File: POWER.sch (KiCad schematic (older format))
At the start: 34 parts, among them U201 TPS61021A, U402 MAX1555

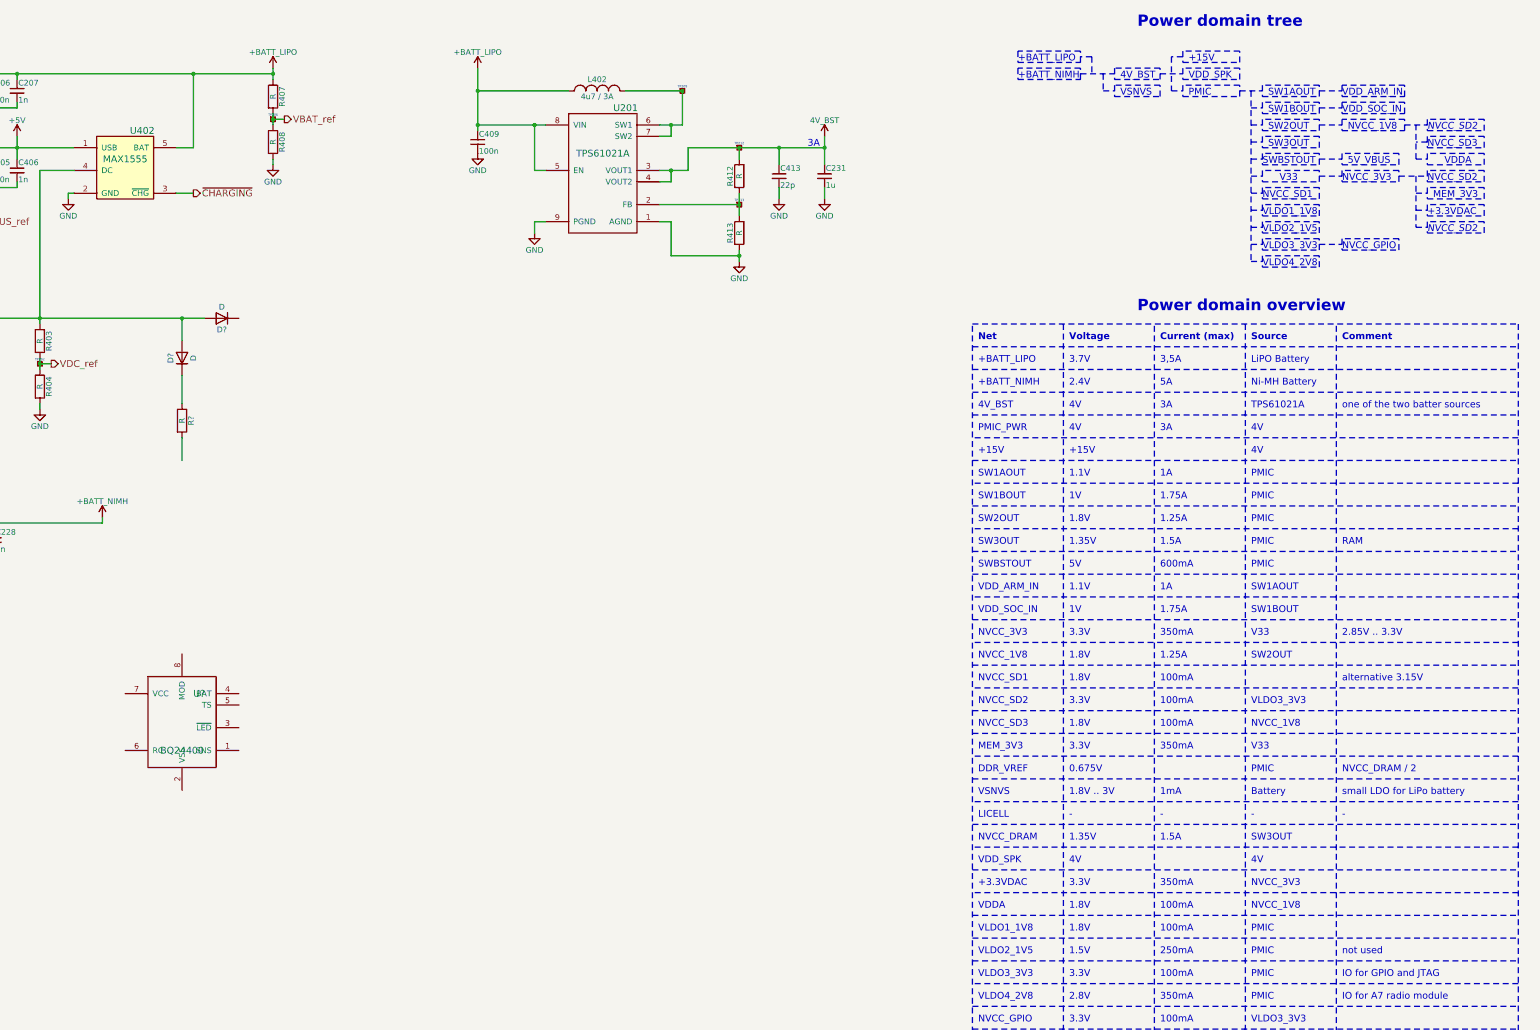
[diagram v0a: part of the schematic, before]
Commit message: on battery charging circuit for NiMH battery
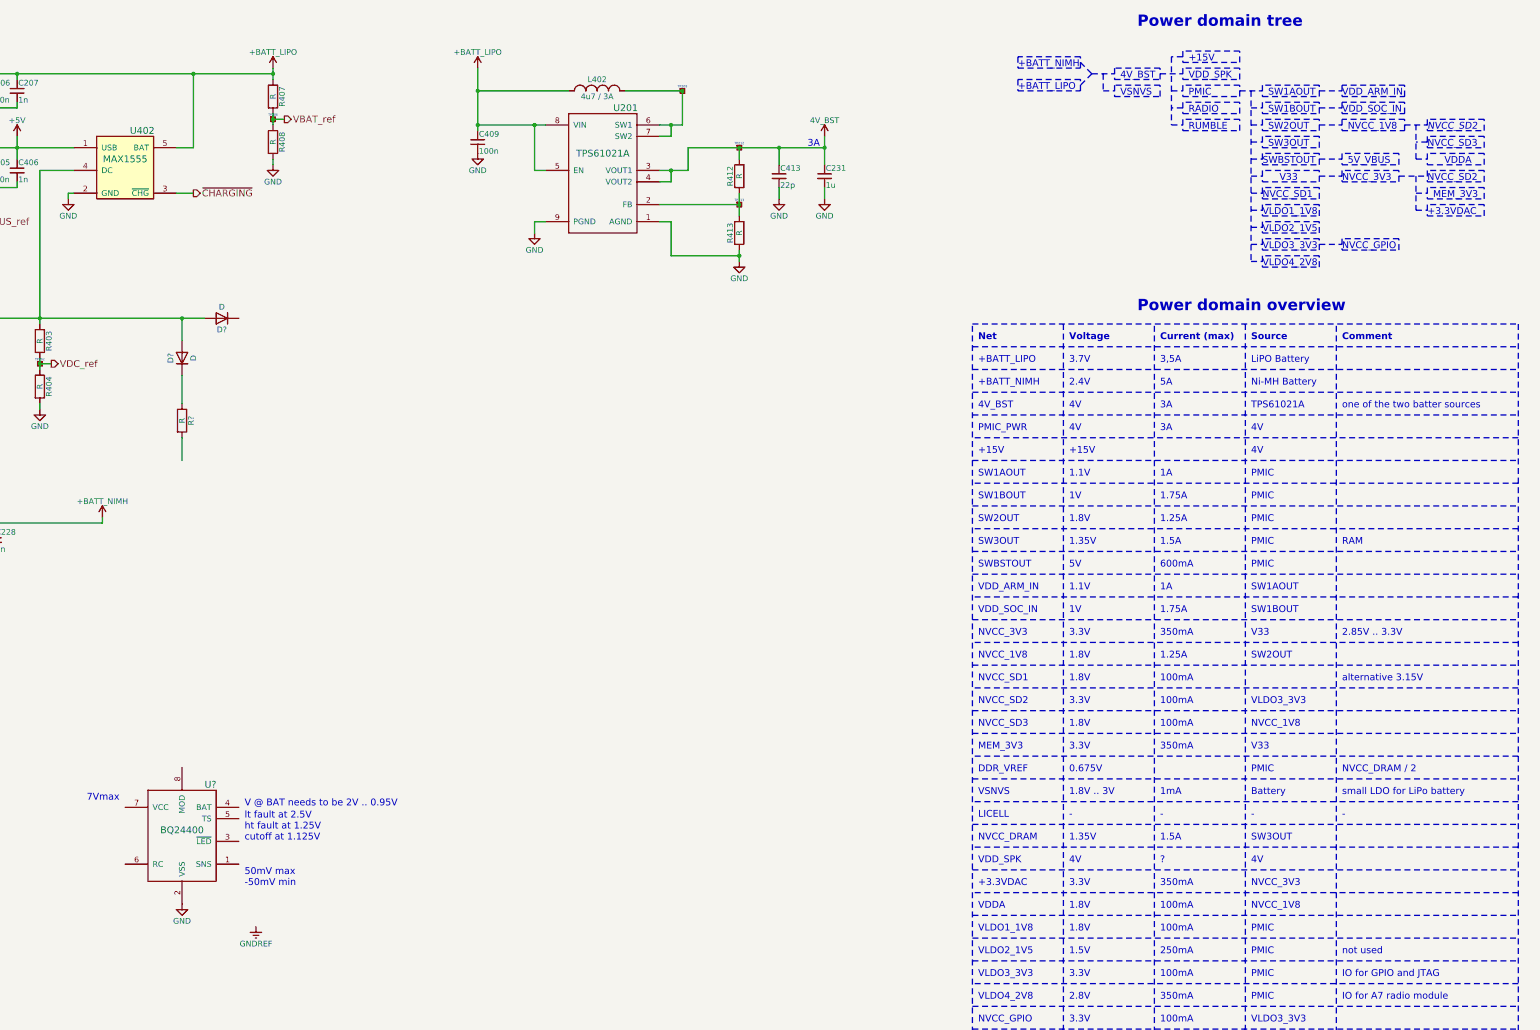
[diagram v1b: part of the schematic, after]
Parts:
- removed U?: BQ24400, symbol BQ24400
- added U?: BQ24400, symbol BQ24400
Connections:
- net GND: now also U?.2 (VSS)
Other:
- note added: "50mV max\n-50mV min"
- note added: "7Vmax"
- note added: "?"
- note added: "RADIO"
- note added: "RUMBLE"
- note added: "V @ BAT needs to be 2V .. 0.95V"
- note added: "lt fault at 2.5V\nht fault at 1.25V\ncutoff at 1.125V\n"
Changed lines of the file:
@@
-$EndComp
-$Comp
-L BQ24400 U?
-U 1 1 59571401
-P 4200 6900
-F 0 "U?" H 4350 7150 60  0000 C CNN
-F 1 "BQ24400" H 4200 6650 60  0000 C CNN
-F 2 "" H 4200 6900 60  0001 C CNN
-F 3 "" H 4200 6900 60  0001 C CNN
-	1    4200 6900
-	1    0    0    -1
 $EndComp
 $Comp
@@
 Text Notes 13600 8150 0    60   ~ 0
 4V
-Text Notes 11550 1100 0    60   ~ 0
+Text Notes 11550 1350 0    60   ~ 0
 +BATT_LIPO
-Text Notes 11550 1250 0    60   ~ 0
+Text Notes 11550 1150 0    60   ~ 0
 +BATT_NIMH
 Text Notes 12450 1250 0    60   ~ 0
@@
 Text Notes 14400 9350 0    60   ~ 0
 IO for A7 radio module
-Text Notes 15150 2600 0    60   Italic 0
-NVCC_SD2
 Text Notes 12600 800  0    99   ~ 20
 Power domain tree
@@
 	3500 5150 3500 5100
 Wire Notes Line
-	12100 1200 12400 1200
+	12200 1200 12400 1200
 Wire Notes Line
 	12400 1150 12400 1250
@@
 	13000 1050 12900 1050
 Wire Notes Line
-	12900 1050 12900 1350
+	12900 1050 12900 1650
 Wire Notes Line
 	12900 1350 13000 1350
@@
 	15050 1950 15050 1650
 Wire Notes Line
-	15050 2100 15050 2550
-Wire Notes Line
-	15050 2550 15150 2550
-Wire Notes Line
-	15150 2500 15150 2600
-Wire Notes Line
-	15150 2600 15650 2600
-Wire Notes Line
-	15650 2600 15650 2500
-Wire Notes Line
-	15650 2500 15150 2500
-Wire Notes Line
-	11550 1100 12100 1100
-Wire Notes Line
-	12100 1100 12100 1000
-Wire Notes Line
-	12100 1000 11550 1000
-Wire Notes Line
-	11550 1000 11550 1100
-Wire Notes Line
-	11550 1150 11550 1250
-Wire Notes Line
-	11550 1250 12100 1250
-Wire Notes Line
-	12100 1250 12100 1150
-Wire Notes Line
-	12100 1150 11550 1150
-Wire Notes Line
-	12200 1050 12100 1050
-Wire Notes Line
-	12200 1050 12200 1200
+	11550 1350 12100 1350
+Wire Notes Line
+	12100 1350 12100 1250
+Wire Notes Line
+	12100 1250 11550 1250
+Wire Notes Line
+	11550 1250 11550 1350
+Wire Notes Line
+	11550 1050 11550 1150
+Wire Notes Line
+	11550 1150 12100 1150
+Wire Notes Line
+	12100 1150 12100 1050
+Wire Notes Line
+	12100 1050 11550 1050
+Wire Notes Line
+	12200 1200 12100 1300
+Wire Notes Line
+	12100 1100 12200 1200
 Wire Notes Line
 	11150 3400 15950 3400
@@
 Text Notes 13600 6950 0    60   ~ 0
 NVCC_1V8
+Text Notes 13050 1550 0    60   ~ 0
+RADIO
+Wire Notes Line
+	13000 1500 12900 1500
+Wire Notes Line
+	13000 1450 13000 1550
+Wire Notes Line
+	13000 1550 13500 1550
+Wire Notes Line
+	13500 1550 13500 1450
+Wire Notes Line
+	13500 1450 13000 1450
+Text Notes 13050 1700 0    60   ~ 0
+RUMBLE
+Wire Notes Line
+	12900 1650 13000 1650
+Wire Notes Line
+	13000 1600 13000 1700
+Wire Notes Line
+	13000 1700 13500 1700
+Wire Notes Line
+	13500 1700 13500 1600
+Wire Notes Line
+	13500 1600 13000 1600
+Wire Notes Line
+	15050 2100 15050 2400
+Text Notes 12800 8150 0    60   ~ 0
+?
+$Comp
+L BQ24400 U?
+U 1 1 595CC806
+P 4200 7900
+F 0 "U?" H 4450 8350 60  0000 C CNN
+F 1 "BQ24400" H 4200 7950 60  0000 C CNN
+F 2 "" H 4850 7850 60  0001 C CNN
+F 3 "" H 4850 7850 60  0001 C CNN
+	1    4200 7900
+	1    0    0    -1
+$EndComp
+Text Notes 4750 7650 0    60   ~ 0
+V @ BAT needs to be 2V .. 0.95V
+Text Notes 4750 8350 0    60   ~ 0
+50mV max\n-50mV min
+Text Notes 3650 7600 2    60   ~ 0
+7Vmax
+Text Notes 4750 7950 0    60   ~ 0
+lt fault at 2.5V\nht fault at 1.25V\ncutoff at 1.125V\n
+$Comp
+L GND #PWR?
+U 1 1 595CEE09
+P 4200 8500
+F 0 "#PWR?" H 4200 8250 50  0001 C CNN
+F 1 "GND" H 4200 8350 50  0000 C CNN
+F 2 "" H 4200 8500 50  0000 C CNN
+F 3 "" H 4200 8500 50  0000 C CNN
+	1    4200 8500
+	1    0    0    -1
+$EndComp
+$Comp
+L GNDREF #PWR?
+U 1 1 595CF102
+P 4850 8700
+F 0 "#PWR?" H 4850 8450 50  0001 C CNN
+F 1 "GNDREF" H 4850 8550 50  0000 C CNN
+F 2 "" H 4850 8700 50  0000 C CNN
+F 3 "" H 4850 8700 50  0000 C CNN
+	1    4850 8700
+	1    0    0    -1
+$EndComp
 $EndSCHEMATC

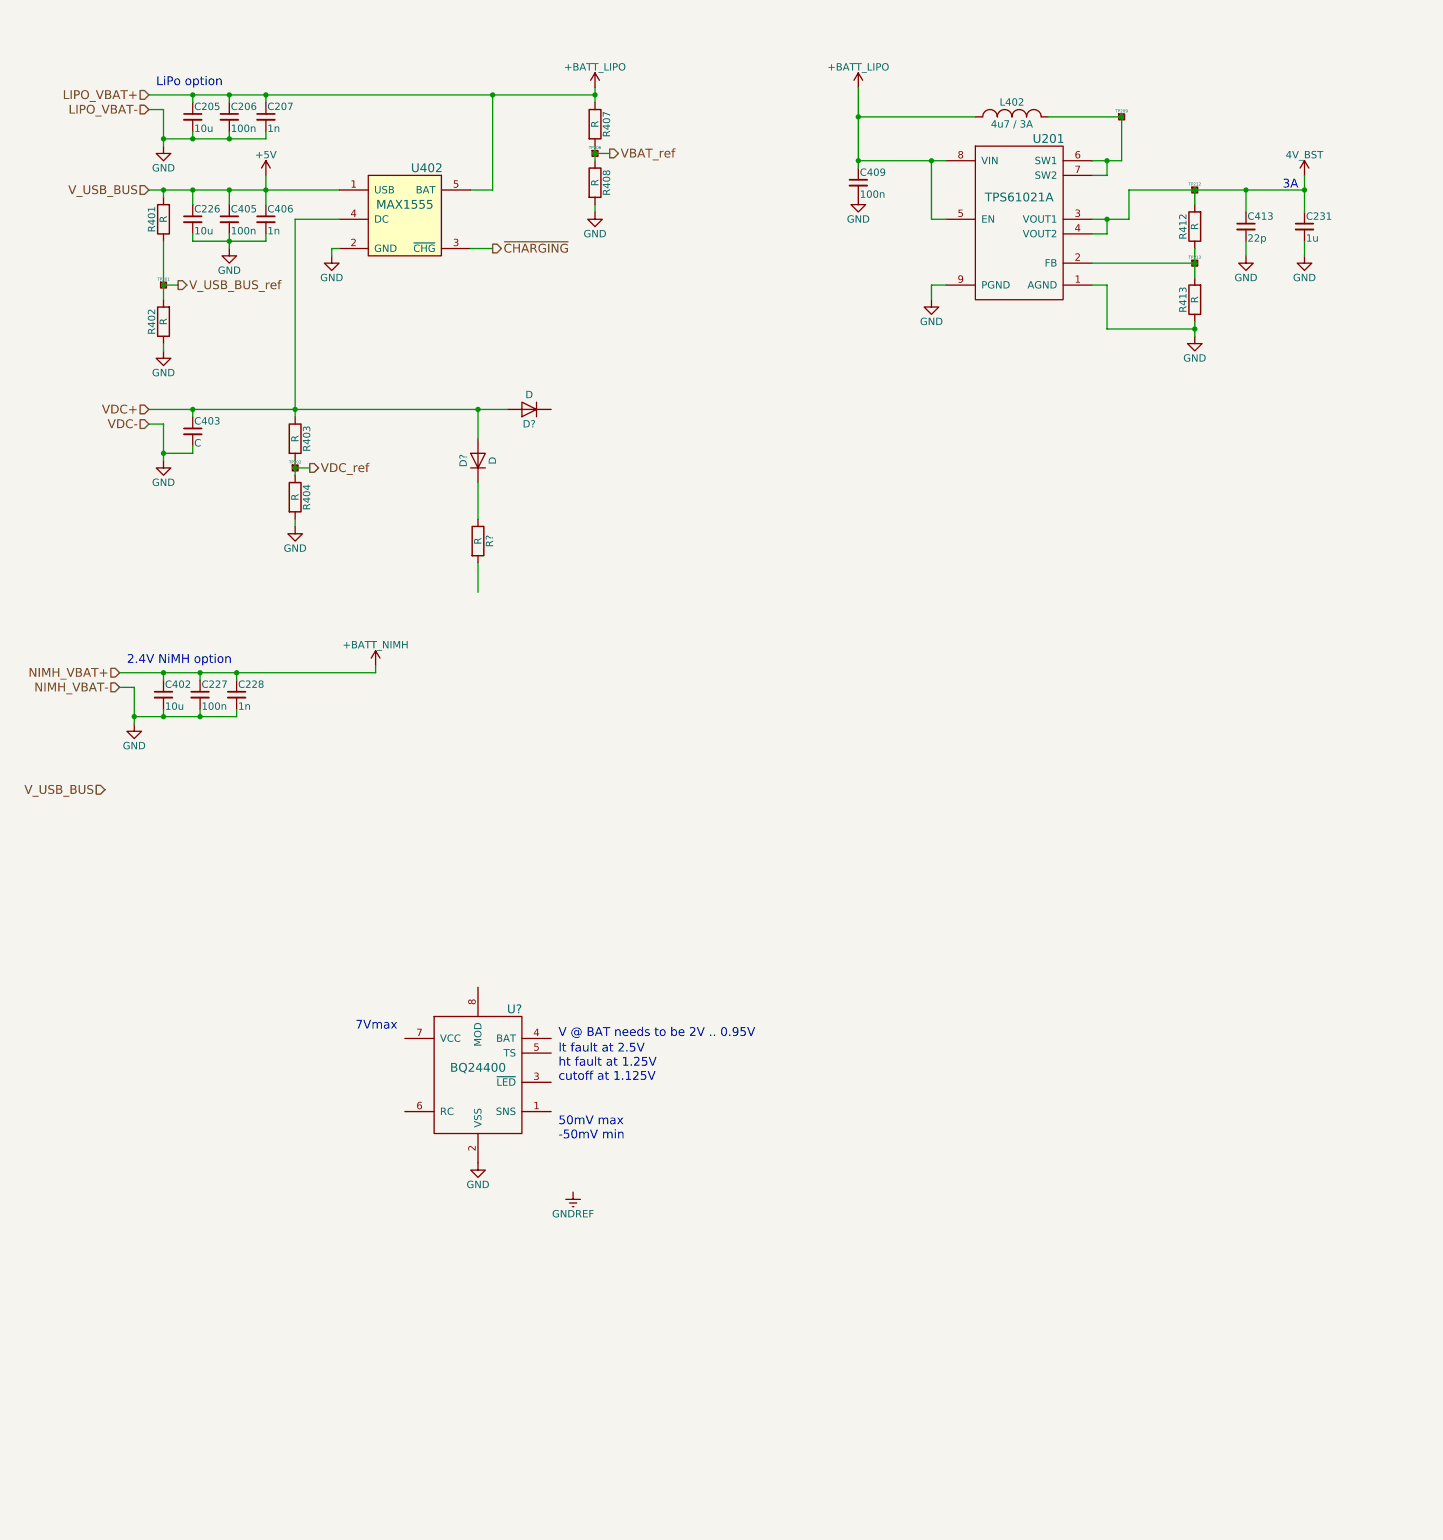
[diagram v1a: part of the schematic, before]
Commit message: Changed several voltage rail connections Removed non existing rails Added circuit for NiMH charging
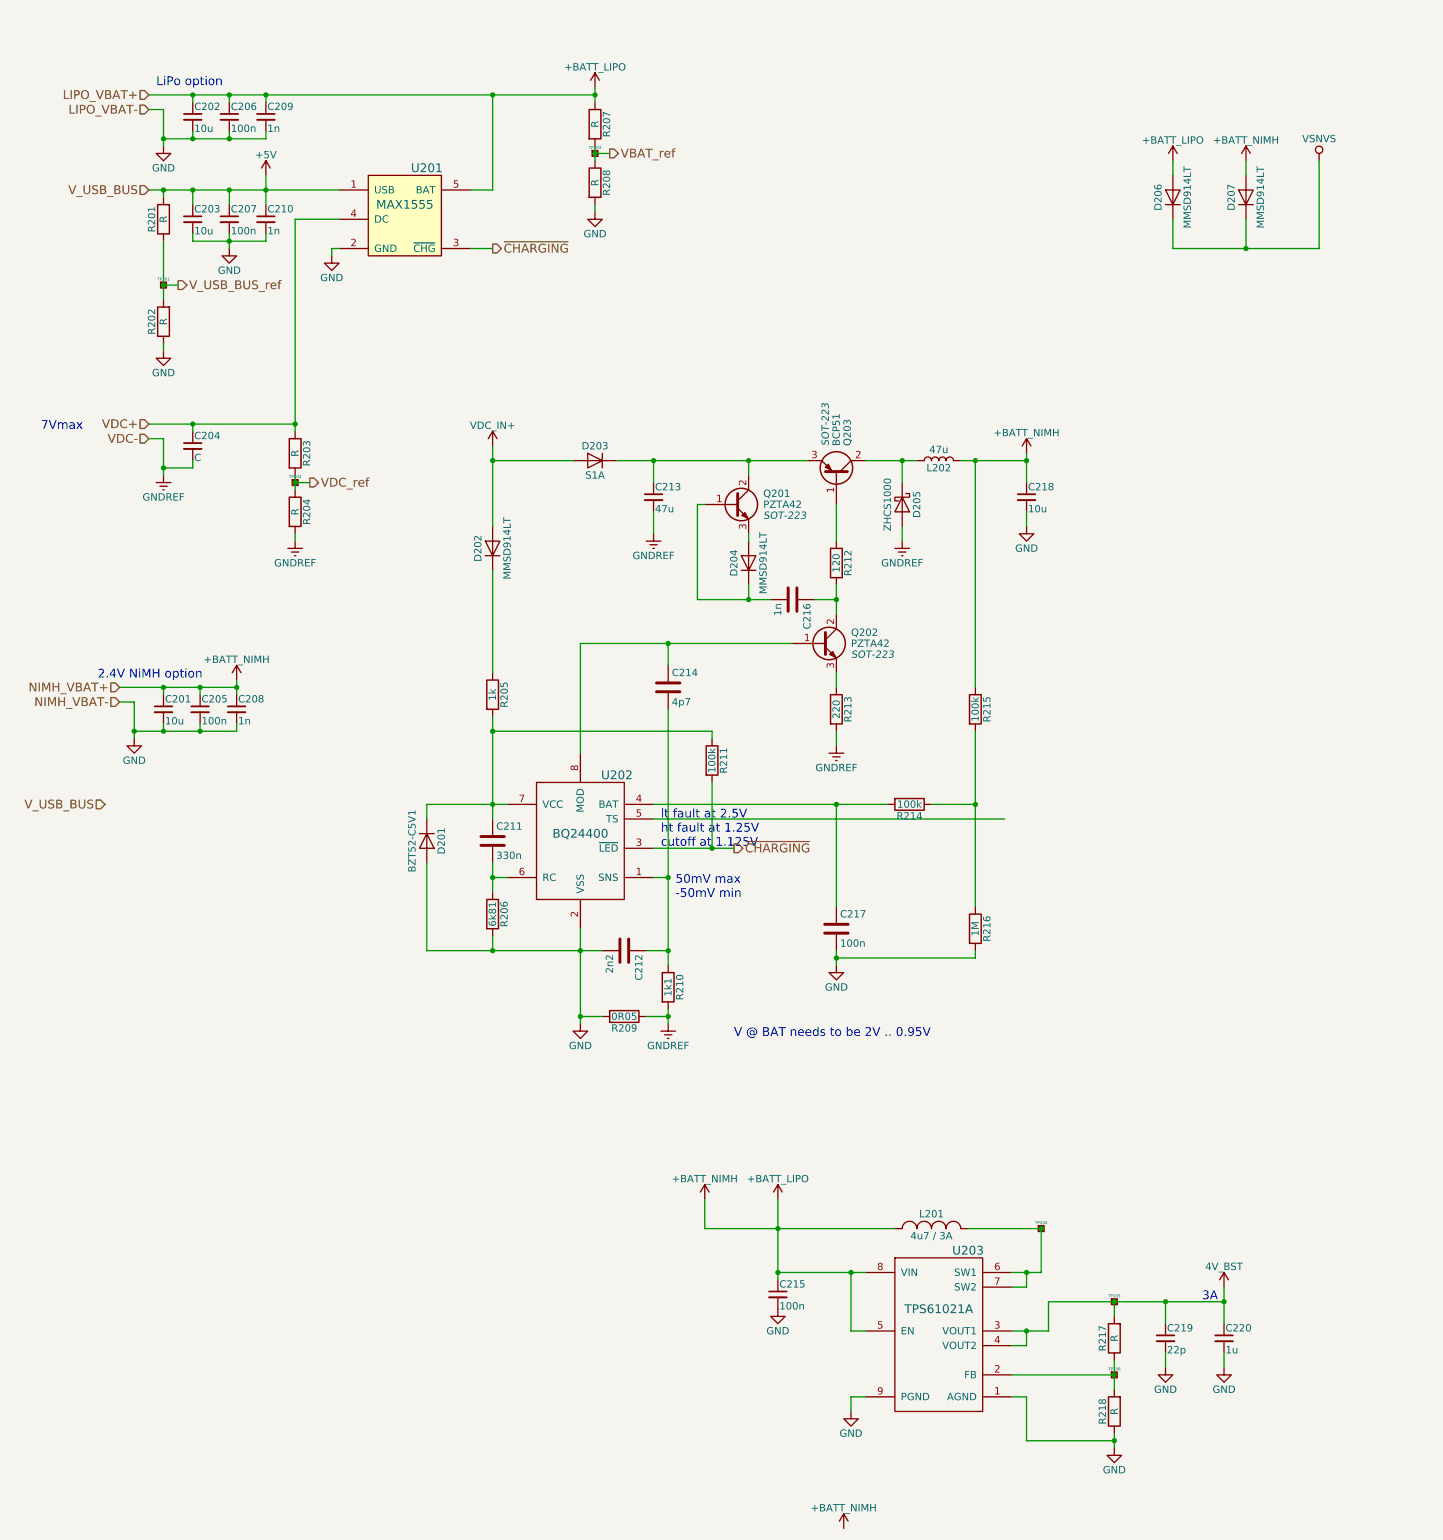
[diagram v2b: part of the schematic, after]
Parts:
- removed D? (x2): D, symbol D
- removed R?: R, Resistors_SMD:R_0603, symbol R
- added C211: 330n, symbol C
- added C212: 2n2, symbol C
- added C213: 47u, Capacitors_SMD:C_0603, symbol C_Small
- added C214: 4p7, symbol C
- added C216: 1n, symbol C
- added C217: 100n, symbol C
- added C218: 10u, Capacitors_SMD:C_0603, symbol C_Small
- added D201: BZT52-C5V1, symbol D
- added D202, D204, D206, D207: MMSD914LT, symbol D
- added D203: S1A, symbol D
- added D205: ZHCS1000, symbol D_Schottky
- added L202: 47u, symbol L
- added Q201, Q202: PZTA42, SOT-223, symbol PZTA42
- added Q203: BCP51, SOT-223, symbol BCP51
- added R205: 1k, Resistors_SMD:R_0603, symbol R
- added R206: 6k81, symbol R
- added R209: 0R05, symbol R
- added R210: 1k1, symbol R
- added R211: 100k, Resistors_SMD:R_0603, symbol R
- added R212: 120, symbol R
- added R213: 220, symbol R
- added R214, R215: 100k, symbol R
- added R216: 1M, symbol R
- gave numbers to parts that had none: 1
- renumbered C402 to C201, C205 to C202, C226 to C203, C403 to C204, C227 to C205, C405 to C207, C228 to C208, C207 to C209, C406 to C210, C409 to C215, C413 to C219, C231 to C220, L402 to L201, R401 to R201, R402 to R202, R403 to R203, R404 to R204, R407 to R207, R408 to R208, R412 to R217, R413 to R218, TP206 to TP203, TP209 to TP204, TP212 to TP205, TP213 to TP206, U402 to U201, U201 to U203
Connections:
- net +BATT_NIMH is gone; now on net +BATT_LIPO: C201.1, C205.1, C208.1
- net +BATT_LIPO: now also C218.1, D206.2 (A), D207.2 (A), L202.2, R215.1
- net GND: now also C212.2, C217.2, C218.2, D201.2 (A), R206.2, R209.2, R216.2; no longer C204.2, R204.2
- net GNDREF: now also C204.2, R204.2, C213.2, D205.2 (A), R209.1, R210.2, R213.2
- net ~CHARGING: now also U202.3 (~LED), R211.2
- net at U202.1 (SNS): now also C212.1, C214.2, R210.1
- net at U202.4 (BAT): now also C217.1, R214.2
- net at U202.6 (RC): now also C211.2, R206.1
- net at U202.7 (VCC): now also C211.1, D201.1 (K), R205.2, R211.1
- net at U202.8 (MOD): now also C214.1, Q202.1 (B)
- new net: Q203.1 (B), R212.1
- new net: D205.1 (K), L202.1, Q203.2 (C)
- new net: C213.1, D203.1 (K), Q201.2 (C), Q203.3 (E)
- new net: C216.2, D204.1 (K), Q201.1 (B)
- new net: D204.2 (A), Q201.3 (E)
- new net: C216.1, Q202.2 (C), R212.2
- new net: Q202.3 (E), R213.1
- new net: R214.1, R215.2, R216.1
- new net: D202.1 (K), R205.1
- new net VDC_IN+: D202.2 (A), D203.2 (A)
- new net VSNVS: D206.1 (K), D207.1 (K)
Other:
- moved on the sheet: C201, C204, C205, C208, C215, C219, C220, L201, R203, R204, R217, R218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
